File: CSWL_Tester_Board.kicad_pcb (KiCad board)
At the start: 2 copper layers, 125.5 x 98 mm, 180 parts, among them J1 DB9_Female ID09S33E4GV00LF, J10 Conn_01x03_Male, J11 Conn_01x02, J12 Conn_01x03, J13 Conn_01x02, J14 Conn_01x04, J15 SPI1, J16 Conn_02x10_Odd_Even, J17 Conn_01x02, J18 Conn_01x02, J19 Conn_01x02, J2 Conn_01x04, J20 Conn_01x02, J21 Fix hole, J22 Conn_01x02, J23 Conn_01x03, J24 Conn_01x02, J25 USB_B_Micro, J26 Conn_01x04, J27 Conn_01x10, J28 Fix hole, J29 Fix hole, J3 Conn_01x04, J30 Fix hole, J31 Conn_Coaxial_Power, J4 Conn_01x04, J5 DB9_Female ID09S33E4GV00LF, J6 Conn_01x04, J7 Conn_01x04, J8 DB9_Female ID09S33E4GV00LF, J9 Conn_Coaxial_Power, K1 G6SU-2 DC5, K2 G6SU-2 DC5, K3 G6SU-2 DC5, K4 G6SU-2 DC5, K5 G6SU-2 DC5, Q1 DMG2301L, Q10 2N7002LT1G, Q11 2N7002LT1G, Q12 DMG2301L, Q13 2N7002LT1G, Q14 DMG2301L, Q2 DMG2301L, Q3 DMG2301L, Q4 2N7002LT1G, Q5 2N7002LT1G, Q6 2N7002LT1G, Q7 DMG2301L, Q8 DMG2301L, Q9 2N7002LT1G, U1 MAX3221EIPW, U10 EL817-S1-A (NC), U2 STM32F103RCT6, U3 MAX3221EIPW, U4 MCP1700T-3302E_TT, U5 MAX3221EIPW, U6 EL817-S1-A (NC), U7 EL817-S1-A (NC), U8 EL817-S1-A (NC), U9 EL817-S1-A (NC), Y1 8MHz

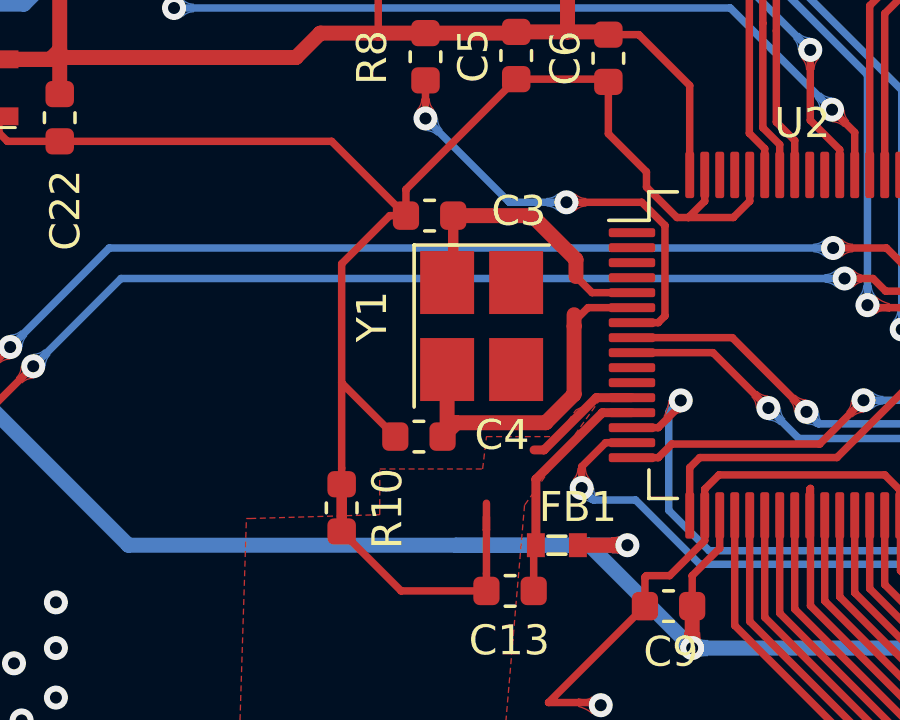
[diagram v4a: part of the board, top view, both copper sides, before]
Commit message: Ruan: change the crystal component
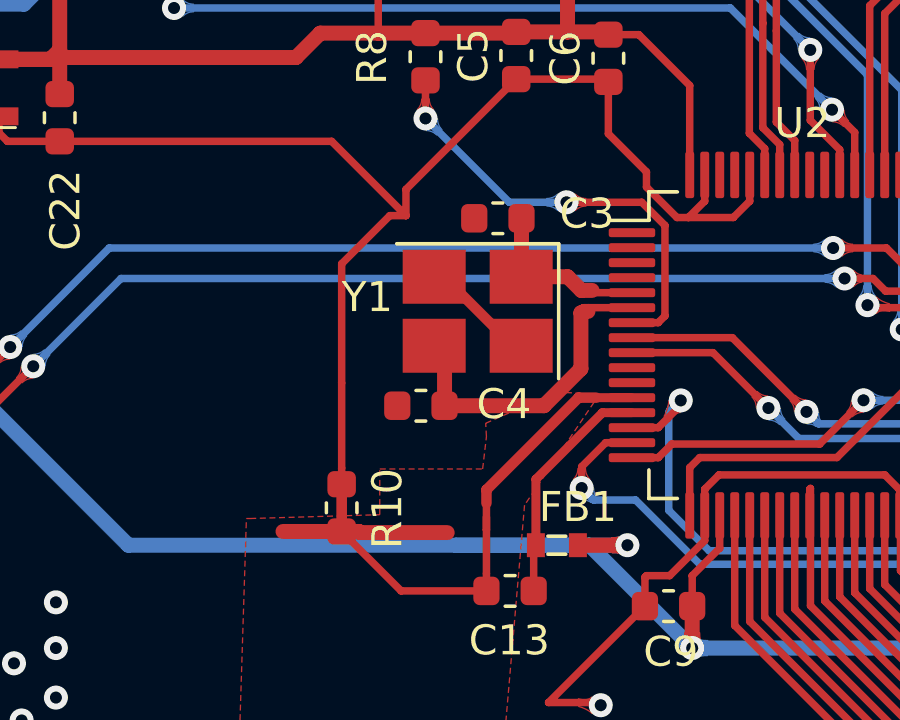
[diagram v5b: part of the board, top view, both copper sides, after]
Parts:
- Y1: value 8MHz -> Crystal_GND24
- moved C3 2.28 mm to (75.8, 71.7)
- moved C4 1.03 mm to (73.3, 77.9)
- moved Y1 0.51 mm to (75.1, 74.8), turned to 180 degrees
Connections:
- Y1 pad 2: Net-(C4-Pad2) -> GND
- Y1 pad 3: (no net) -> Net-(C4-Pad2)
- Y1 pad 4: (no net) -> GND
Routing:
- net GNDA: track 13.0 -> 22.5 mm
- net Net-(C3-Pad2): track 9.67 -> 5.83 mm
- net Net-(C4-Pad2): track 12.2 -> 10.8 mm
- net GND: track 693.8 -> 695.1 mm

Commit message: Ruan: modify the coper zone
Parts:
- C3, C4: value 20pF -> 22pF
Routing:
- net GND: track 695.1 -> 709.2 mm
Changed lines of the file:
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@@
     (thickness 1.6)
     (drawings 74)
-    (tracks 2112)
+    (tracks 2122)
     (zones 0)
     (modules 180)
@@
       (effects (font (size 1 1) (thickness 0.15)))
     )
-    (fp_text value 20pF (at 0 1.43) (layer F.Fab)
+    (fp_text value 22pF (at 0 1.43) (layer F.Fab)
       (effects (font (size 1 1) (thickness 0.15)))
     )
@@
       (effects (font (size 1 1) (thickness 0.15)))
     )
-    (fp_text value 20pF (at 0 1.43) (layer F.Fab)
+    (fp_text value 22pF (at 0 1.43) (layer F.Fab)
       (effects (font (size 1 1) (thickness 0.15)))
     )
@@
   (segment (start 73.6959 73.6022) (end 74.020902 73.6022) (width 0.35) (layer F.Cu) (net 6))
   (segment (start 74.020902 73.6022) (end 76.320902 75.9022) (width 0.35) (layer F.Cu) (net 6))
+  (segment (start 43.276 68.58) (end 39.7764 68.58) (width 1) (layer B.Cu) (net 6))
+  (segment (start 43.276 66.73) (end 43.2816 66.7244) (width 1) (layer B.Cu) (net 6))
+  (segment (start 43.276 68.58) (end 43.276 66.73) (width 1) (layer B.Cu) (net 6))
+  (segment (start 43.2816 66.7244) (end 43.2816 64.4398) (width 1) (layer B.Cu) (net 6))
+  (segment (start 44.876 68.58) (end 44.9014 68.6054) (width 1) (layer B.Cu) (net 6))
+  (segment (start 43.276 68.58) (end 44.876 68.58) (width 1) (layer B.Cu) (net 6))
+  (segment (start 44.9014 68.6054) (end 45.9486 68.6054) (width 1) (layer B.Cu) (net 6))
+  (segment (start 43.276 70.43) (end 43.2816 70.4356) (width 1) (layer B.Cu) (net 6))
+  (segment (start 43.276 68.58) (end 43.276 70.43) (width 1) (layer B.Cu) (net 6))
+  (segment (start 43.2816 70.4356) (end 43.2816 72.3138) (width 1) (layer B.Cu) (net 6))
   (segment (start 80.28876 74.6325) (end 78.82209 74.6325) (width 0.25) (layer F.Cu) (net 7))
   (segment (start 74.041 76.2473) (end 73.6959 75.9022) (width 0.5) (layer F.Cu) (net 7))
@@
   (segment (start 133.3525 79.2251) (end 133.3378 79.2398) (width 0.25) (layer F.Cu) (net 188))
   (zone (net 128) (net_name GNDS) (layer F.Cu) (hatch edge 0.508)
+    (priority 1)
     (connect_pads (clearance 0.508))
     (min_thickness 0.254)
-    (fill yes (arc_segments 32) (thermal_gap 0.508) (thermal_bridge_width 0.508))
+    (fill yes (arc_segments 32) (thermal_gap 0.508) (thermal_bridge_width 0.508) (smoothing fillet) (radius 2))
     (polygon
       (pts
@@
     (connect_pads (clearance 0.508))
     (min_thickness 0.254)
-    (fill yes (arc_segments 32) (thermal_gap 0.508) (thermal_bridge_width 0.508))
+    (fill yes (arc_segments 32) (thermal_gap 0.508) (thermal_bridge_width 0.508) (smoothing fillet) (radius 2))
     (polygon
       (pts
@@
     (connect_pads (clearance 0.508))
     (min_thickness 0.254)
-    (fill yes (arc_segments 32) (thermal_gap 0.508) (thermal_bridge_width 0.508))
+    (fill yes (arc_segments 32) (thermal_gap 0.508) (thermal_bridge_width 0.508) (smoothing fillet) (radius 2))
     (polygon
       (pts
@@
     )
   )
-  (zone (net 0) (net_name "") (layer F.Cu) (hatch edge 0.508)
-    (connect_pads (clearance 0.508))
-    (min_thickness 0.254)
-    (keepout (tracks allowed) (vias allowed) (copperpour not_allowed))
-    (fill (arc_segments 32) (thermal_gap 0.508) (thermal_bridge_width 0.508))
-    (polygon
-      (pts
-        (xy 78.994 77.343) (xy 77.724 77.343) (xy 76.581 77.2922) (xy 75.8952 77.7875) (xy 75.057 78.359)
-        (xy 75.057 79.756) (xy 75.057 79.883) (xy 71.755 79.883) (xy 71.755 81.407) (xy 67.31 81.407)
-        (xy 67.056 89.916) (xy 76.073 90.17) (xy 76.835 81.28) (xy 77.1779 80.5434) (xy 79.0829 78.5114)
-        (xy 80.645 77.851) (xy 80.772 77.343) (xy 79.248 77.343) (xy 79.248 77.216) (xy 80.899 77.216)
-        (xy 80.645 77.978) (xy 79.1718 78.7146) (xy 77.3938 80.7466) (xy 76.962 81.407) (xy 76.2 90.424)
-        (xy 66.675 90.297) (xy 67.183 81.28) (xy 71.501 81.153) (xy 71.628 79.756) (xy 74.93 79.629)
-        (xy 74.93 78.105) (xy 76.35875 77.1271) (xy 77.61605 77.0509) (xy 78.994 77.216)
-      )
-    )
-  )
-  (zone (net 0) (net_name "") (layers F&B.Cu) (hatch edge 0.508)
-    (connect_pads (clearance 0.508))
-    (min_thickness 0.254)
-    (keepout (tracks allowed) (vias allowed) (copperpour not_allowed))
-    (fill (arc_segments 32) (thermal_gap 0.508) (thermal_bridge_width 0.508))
-    (polygon
-      (pts
-        (xy 130.81 68.453) (xy 156.972 68.453) (xy 157.15615 77.56525) (xy 130.37185 78.21295) (xy 130.5687 68.7197)
-        (xy 130.81 68.58) (xy 130.4036 68.5165) (xy 130.2131 78.50505) (xy 157.2895 77.93355) (xy 157.099 68.326)
-        (xy 130.683 68.326) (xy 130.683 68.453)
-      )
-    )
-  )
   (zone (net 181) (net_name GNDA1) (layer B.Cu) (hatch edge 0.508)
+    (priority 1)
     (connect_pads yes (clearance 0.508))
     (min_thickness 0.254)
-    (fill yes (arc_segments 32) (thermal_gap 0.508) (thermal_bridge_width 0.508))
+    (fill yes (arc_segments 32) (thermal_gap 0.254) (thermal_bridge_width 0.508) (smoothing fillet) (radius 1))
     (polygon
       (pts
@@
   )
   (zone (net 182) (net_name GNDA2) (layer B.Cu) (hatch edge 0.508)
+    (priority 1)
     (connect_pads yes (clearance 0.508))
     (min_thickness 0.254)
-    (fill yes (arc_segments 32) (thermal_gap 0.508) (thermal_bridge_width 0.508))
+    (fill yes (arc_segments 32) (thermal_gap 0.508) (thermal_bridge_width 0.508) (smoothing fillet) (radius 1))
     (polygon
       (pts
@@
   )
   (zone (net 183) (net_name GNDA3) (layer B.Cu) (hatch edge 0.508)
+    (priority 1)
     (connect_pads yes (clearance 0.508))
     (min_thickness 0.254)
-    (fill yes (arc_segments 32) (thermal_gap 0.508) (thermal_bridge_width 0.508))
+    (fill yes (arc_segments 32) (thermal_gap 0.508) (thermal_bridge_width 0.508) (smoothing fillet) (radius 1))
     (polygon
       (pts
@@
   )
   (zone (net 12) (net_name GNDA) (layer F.Cu) (hatch edge 0.508)
+    (priority 1)
     (connect_pads (clearance 0.508))
     (min_thickness 0.254)
-    (fill yes (arc_segments 32) (thermal_gap 0.508) (thermal_bridge_width 0.508))
+    (fill yes (arc_segments 32) (thermal_gap 0.508) (thermal_bridge_width 0.508) (smoothing fillet) (radius 1))
     (polygon
       (pts
